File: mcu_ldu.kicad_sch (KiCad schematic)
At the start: 9 parts

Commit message: v1
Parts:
- gave numbers to parts that had none: 9
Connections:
- net IO25: now reaches IC1.10 (IO25)
- net IO26: now reaches IC1.11 (IO26)
- net IO27: now reaches IC1.12 (IO27)
- net IO14: now reaches IC1.13 (IO14)
- net IO12: now reaches IC1.14 (IO12)
- net IO13: now reaches IC1.16 (IO13)
- net IO15: now reaches IC1.23 (IO15)
- net IO2: now reaches IC1.24 (IO2)
- no-connect marks 7 -> 12
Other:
- note added: "ESP32 Microcontroller"
- moved on the sheet: C1, C2, C3, C4, C5, IC1, R1, SW1, SW2

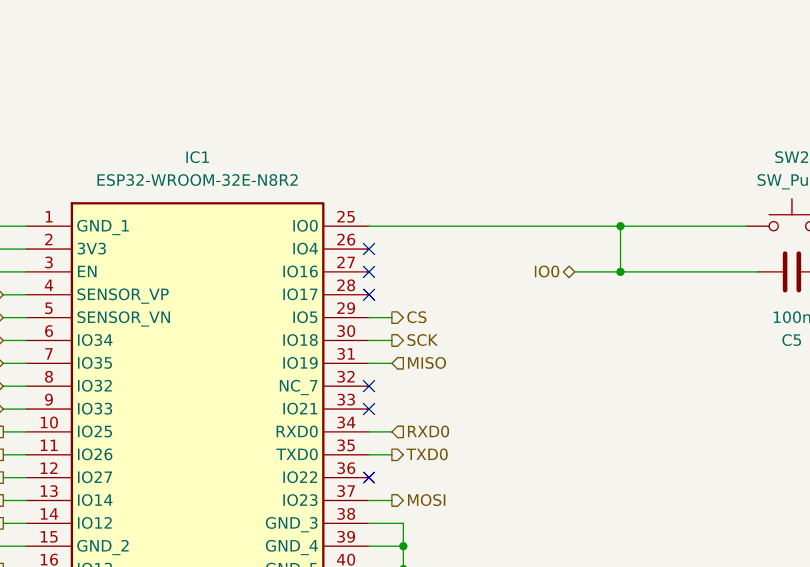
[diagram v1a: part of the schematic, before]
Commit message: LCD Display
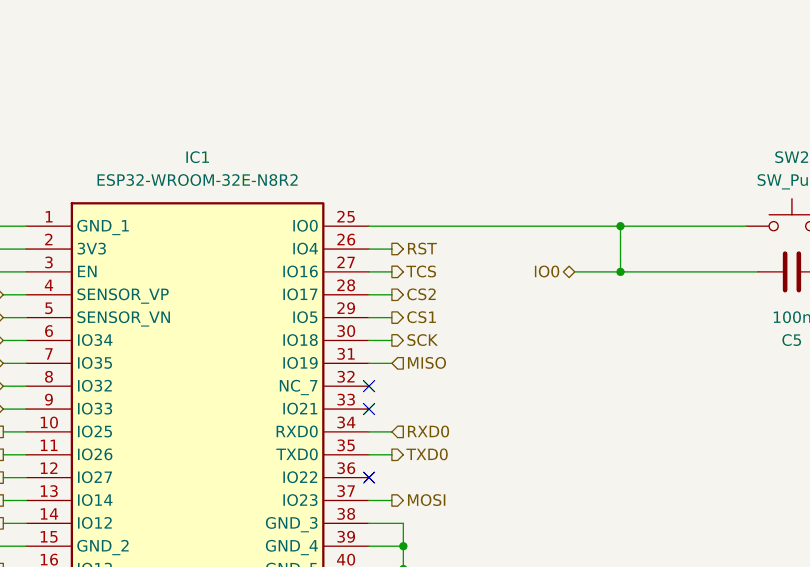
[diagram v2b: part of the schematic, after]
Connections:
- net RST: now reaches IC1.26 (IO4)
- net TCS: now reaches IC1.27 (IO16)
- net CS2: now reaches IC1.28 (IO17)
- net CS renamed CS1
- no-connect marks 12 -> 9
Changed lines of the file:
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@@
-	)
-	(no_connect
-		(at 175.26 83.82)
 	)
 	(no_connect
@@
 	)
 	(no_connect
-		(at 175.26 81.28)
-	)
-	(no_connect
 		(at 137.16 127)
-	)
-	(no_connect
-		(at 175.26 86.36)
 	)
 	(no_connect
@@
 	(wire
 		(pts
+			(xy 175.26 86.36) (xy 177.8 86.36)
+		)
+		(stroke
+			(width 0)
+			(type default)
+		)
+	)
+	(wire
+		(pts
 			(xy 114.3 83.82) (xy 137.16 83.82)
 		)
@@
 	(wire
 		(pts
+			(xy 175.26 81.28) (xy 177.8 81.28)
+		)
+		(stroke
+			(width 0)
+			(type default)
+		)
+	)
+	(wire
+		(pts
 			(xy 179.07 127) (xy 179.07 129.54)
 		)
@@
 		(pts
 			(xy 106.68 58.42) (xy 106.68 60.96)
+		)
+		(stroke
+			(width 0)
+			(type default)
+		)
+	)
+	(wire
+		(pts
+			(xy 175.26 83.82) (xy 177.8 83.82)
 		)
 		(stroke
@@
 		)
 	)
-	(hierarchical_label "CS"
+	(hierarchical_label "CS1"
 		(shape output)
 		(at 177.8 88.9 0)
@@
 		)
 	)
+	(hierarchical_label "CS2"
+		(shape output)
+		(at 177.8 86.36 0)
+		(fields_autoplaced yes)
+		(effects
+			(font
+				(size 1.27 1.27)
+			)
+			(justify left)
+		)
+	)
 	(hierarchical_label "SCK"
 		(shape output)
@@
 		)
 	)
+	(hierarchical_label "TCS"
+		(shape output)
+		(at 177.8 83.82 0)
+		(fields_autoplaced yes)
+		(effects
+			(font
+				(size 1.27 1.27)
+			)
+			(justify left)
+		)
+	)
 	(hierarchical_label "IO39"
 		(shape input)
@@
 		)
 	)
+	(hierarchical_label "RST"
+		(shape output)
+		(at 177.8 81.28 0)
+		(fields_autoplaced yes)
+		(effects
+			(font
+				(size 1.27 1.27)
+			)
+			(justify left)
+		)
+	)

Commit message: passed drc (somehow)
board routing is def cooked
verify:
- boost layout
- usb terminal layout
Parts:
- removed SW1, SW2: SW_Push, symbol Switch:SW_Push
- added SW1, SW2: 1825910-6, footprints:SW4_1825910-B_TEC, symbol button:1825910-6
- C1, C2, C3, C4, C5: footprint (none) -> Capacitor_SMD:C_0603_1608Metric_Pad1.08x0.95mm_HandSolder
- IC1: footprint ESP32WROOM32EN8R2 -> footprints:ESP32WROOM32EN8R2
- R1: footprint (none) -> Resistor_SMD:R_0603_1608Metric
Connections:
- net GND: now also SW1.1, SW1.2, SW2.3, SW2.4
- net IO0: now also SW2.1, SW2.2
- net MCU_EN: now also SW1.3, SW1.4
- net IO15: no longer names the net of IC1.23 (IO15)
- no-connect marks 9 -> 10
